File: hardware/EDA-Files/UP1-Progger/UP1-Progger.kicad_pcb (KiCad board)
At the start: 2 copper layers, 29.2 x 33.7 mm, 10 parts, among them J1 KUPS-Conn, J2 USB_B_Micro, J4 SWD_Interface, J5 ST Link V2 Clone, SW1 Reset, SW2 Bootsel, U1 LDO_3V3_SOT23-3

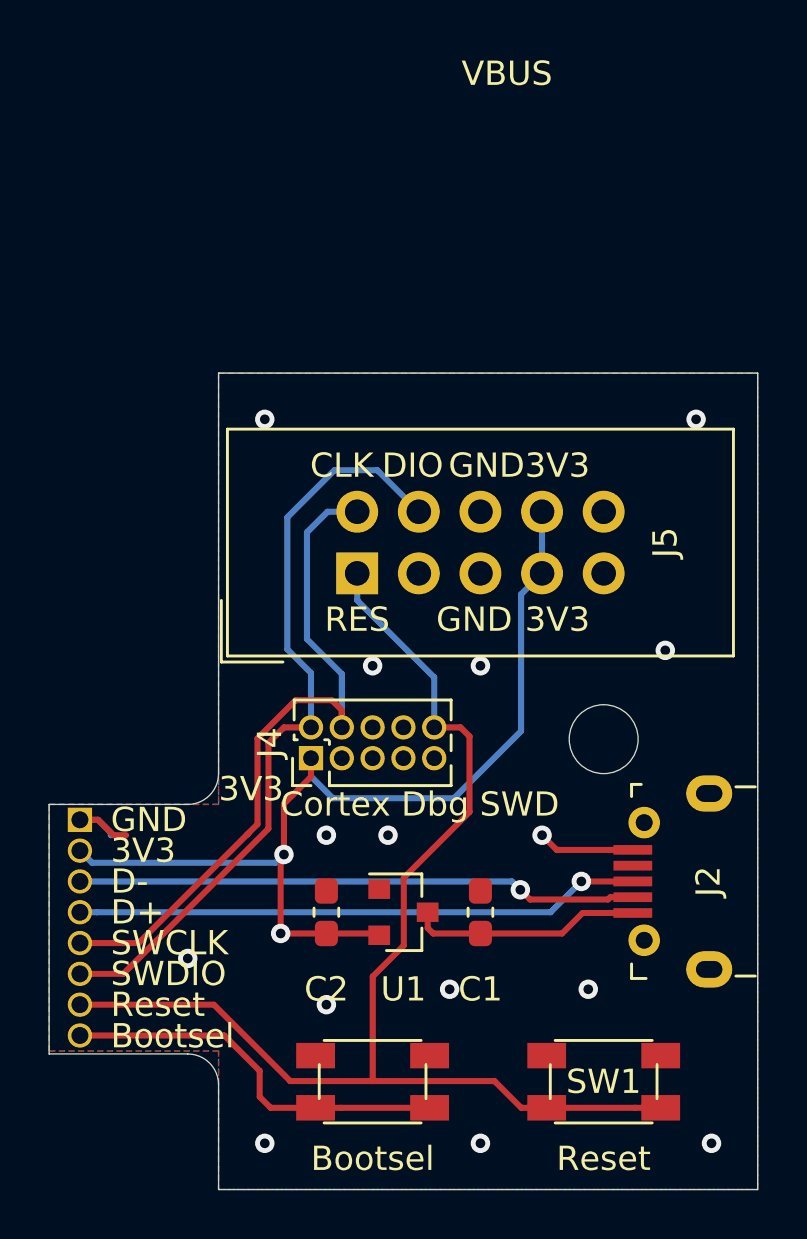
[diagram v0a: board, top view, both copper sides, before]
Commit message: KiCad, add JST 1.25, V01.00
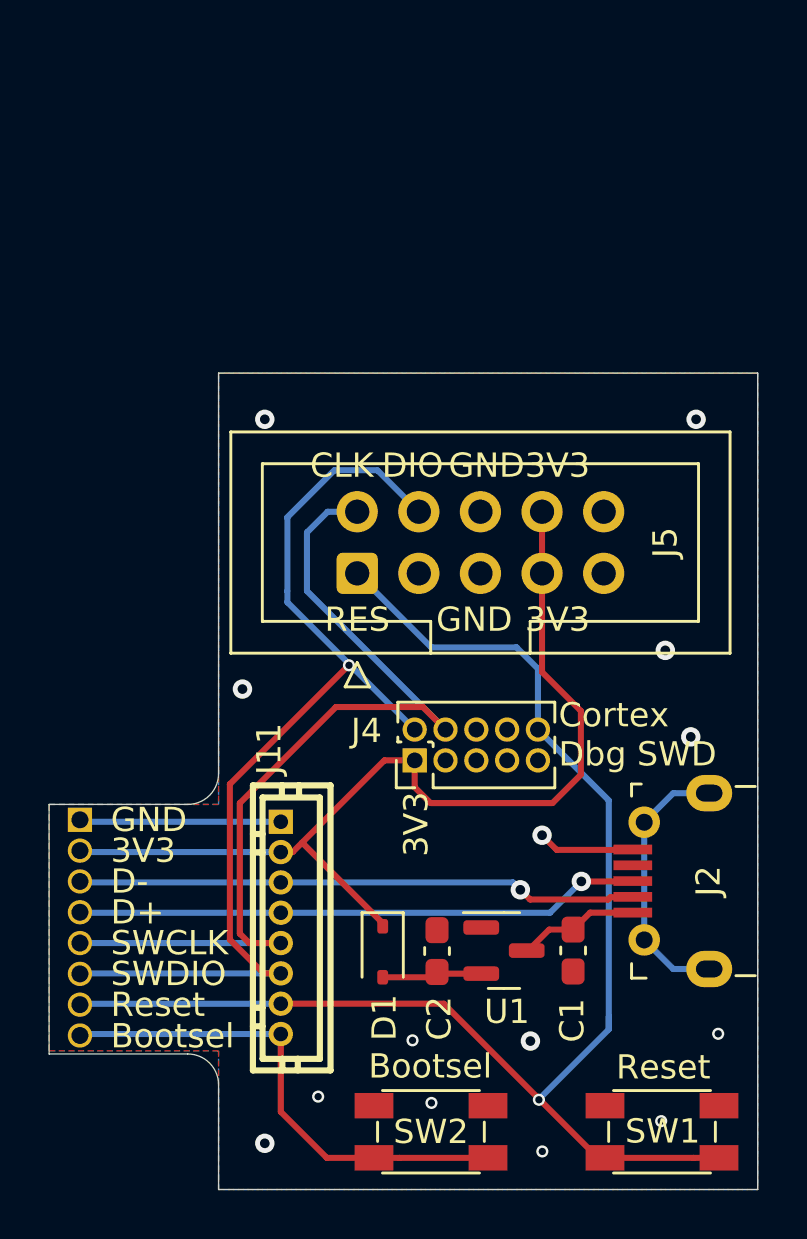
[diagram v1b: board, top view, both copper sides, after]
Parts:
- added D1: 1N5819, Diode_SMD:D_SOD-323, F.Cu at (103.9, 118.5)
- added J11: UP1_Prog_Connector, EasyEDALib:CONN-TH_1.25-8A, F.Cu at (99.7, 117.5)
- C1, C2: value 1uF -> 1u; footprint Capacitor_SMD:C_0603_1608Metric_Pad1.05x0.95mm_HandSolder -> Capacitor_SMD:C_0603_1608Metric_Pad1.08x0.95mm_HandSolder
- J1: value KUPS-Conn -> UP1_Prog_Connector
- J2: footprint sirsydom:USB_Micro-B_JING_C10418 -> DomsKiCADLib:USB_Micro-B_JING_C10418
- SW1, SW2: footprint sirsydom:SW_Push_Xunpu_TS-1089S_Handsolder -> EasyEDAModLib:C455282_SW-SMD_4P-L4.2-W3.3-P2.15-LS5.1_Handsolder
- moved C2 4.83 mm to (106.2, 118.4)
- moved U1 4.44 mm to (108.9, 118.4)
- moved J4 4.28 mm to (105.2, 110.6)
- moved C1 4.13 mm to (111.8, 118.4), turned to -90 degrees
- moved J2 3.40 mm to (116.0, 115.6)
- moved SW1 3.17 mm to (115.4, 125.9)
- moved SW2 3.17 mm to (105.9, 125.9)
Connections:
- C2 pad 1: +3V3 -> Net-(D1-A)
- J1 pad 2: +3V3 -> +3.3V
- J2 pad 4: Net-(J2-Pad4) -> unconnected-(J2-ID-Pad4)
- J2 pad 6: Net-(J2-Pad6) -> unconnected-(J2-Shield-Pad6)
- J4 pad 1: +3V3 -> +3.3V
- J4 pad 6: Net-(J4-Pad6) -> unconnected-(J4-Pin_6-Pad6)
- J4 pad 7: Net-(J4-Pad7) -> unconnected-(J4-Pin_7-Pad7)
- J4 pad 8: Net-(J4-Pad8) -> unconnected-(J4-Pin_8-Pad8)
- J5 pad 10: Net-(J5-Pad10) -> unconnected-(J5-Pin_10-Pad10)
- J5 pad 3: Net-(J5-Pad3) -> unconnected-(J5-Pin_3-Pad3)
- J5 pad 7: +3V3 -> +3.3V
- J5 pad 8: +3V3 -> +3.3V
- J5 pad 9: Net-(J5-Pad9) -> unconnected-(J5-Pin_9-Pad9)
- U1 pad 2: +3V3 -> Net-(D1-A)
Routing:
- net +3V3: track 40.9 -> 0.00 mm, vias 2 -> 0
- net +3.3V: track 0.00 -> 40.4 mm
- net unconnected-(J2-Shield-Pad6): track 0.00 -> 11.2 mm
- net SWDIO: track 31.8 -> 42.1 mm, vias 0 -> 1
- net SWCLK: track 29.1 -> 38.9 mm
- net Reset: track 50.8 -> 58.7 mm, vias 0 -> 1
- net +5V: track 9.55 -> 4.96 mm
- net Bootsel: track 16.3 -> 20.8 mm
- net GND: track 7.76 -> 12.3 mm, vias 15 -> 14
- net Net-(D1-A): track 0.00 -> 4.12 mm
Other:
- outline, holes or cut-outs redrawn
- net class Default removed
- rule pad_to_mask_clearance: 0 -> 0.038
- board text added: "Ing-Dom, 2023"
- board text added: "V01.00"
- board text removed: "SirSydom, 2022"
- board text removed: "V00.20"
- board text removed: "VBUS"

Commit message: wip progger
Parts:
- removed the G*** at (103.5, 116.8)
- added G***: LOGO, OpenKNX:OpenKNX_Logo_10x10, B.Cu at (113.0, 106.1)
- added G***: LOGO, OpenKNX:CC-BY-NY-SA_12x4, B.Cu at (103.9, 104.3)
- added J3: Conn_01x03, Connector_PinHeader_2.54mm:PinHeader_1x03_P2.54mm_Vertical, F.Cu at (116.4, 102.7)
- added REF**: JLCPCB_Tooling_hole, DomsKiCADLib:JLCPCB_Tooling_hole, F.Cu at (115.2, 121.5)
- added REF**: JLCPCB_Tooling_hole, DomsKiCADLib:JLCPCB_Tooling_hole, F.Cu at (98.7, 102.5)
- J5: moved to B.Cu
- moved J5 12.0 mm to (113.3, 96.9)
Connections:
- J5 pad 1: Reset -> +3.3V
- J5 pad 10: unconnected-(J5-Pin_10-Pad10) -> GND
- J5 pad 2: SWCLK -> Net-(J3-Pin_2)
- J5 pad 3: unconnected-(J5-Pin_3-Pad3) -> D+
- J5 pad 4: SWDIO -> D-
- J5 pad 5: GND -> SWCLK
- J5 pad 6: GND -> SWDIO
- J5 pad 7: +3.3V -> Reset
- J5 pad 8: +3.3V -> Bootsel
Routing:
- net Bootsel: track 20.8 -> 52.2 mm
- net D-: track 23.1 -> 46.8 mm
- net D+: track 23.3 -> 42.5 mm
- net GND: track 12.3 -> 28.5 mm, vias 14 -> 15
- net +5V: track 4.96 -> 18.4 mm
- net Net-(J3-Pin_2): track 0.00 -> 13.0 mm
- net +3.3V: track 40.4 -> 49.2 mm
- net Reset: track 58.7 -> 63.1 mm, vias 1 -> 2
- net SWCLK: track 38.9 -> 37.6 mm
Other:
- board size 29.2 x 33.7 mm -> 29.2 x 35.2 mm
- board text added: "5V"
- board text added: "BL"
- board text added: "NC"
- board text added: "Res"
- board text added: "UP1-Progger V01.10 by Ing-Dom, 2024"
- board text added: "V2"
- board text removed: "Ing-Dom, 2023"
- board text removed: "RES"
- board text removed: "UP1-Progger"
- board text removed: "V01.00"
